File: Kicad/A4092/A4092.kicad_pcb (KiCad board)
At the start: 4 copper layers, 175.6 x 122.1 mm, 129 parts, among them CN1 Zorro3, J1 5749721-7, J2 5749721-7, J3 TO-LED, J4 TO-MB, J5 TO-A3000-LED, J6 TO-A3000-MB, J8 Conn_01x06_Pin, U1 SN74ABT16543DGGR, U10 DS21S07A, U11 DS21S07A, U12 DS21S07A, U13 W25X40CLSN, U2 SN74ABT16543DGGR, U3 SN74ABT16543DGGR, U4 SN74ABT16543DGGR, U5 74LVC07APW_118, U6 SN74ABT16245ADGGR, U7 AMS1117-3.3, U8 XC95144XL-TQ144, U9 LSI53C770 SCSI Host Controller, Y1 Abracon ACO-50MHz, Y2 Abracon ACO-40MHz

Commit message: Routing
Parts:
- moved R64 6.00 mm to (196.5, 124.0)
- moved R66 3.00 mm to (196.5, 119.5)
- moved R68 3.00 mm to (196.5, 116.5)
- moved R65 1.50 mm to (196.5, 122.5)
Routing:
- net D13: track 15.1 -> 77.5 mm, vias 0 -> 1
- net SBG: track 59.2 -> 0.00 mm, vias 1 -> 0
- net SCDATP0: track 39.5 -> 93.2 mm, vias 1 -> 2
- net A28: track 47.2 -> 99.6 mm, vias 2 -> 3
- net PLD_FC2: track 95.2 -> 147.4 mm, vias 3 -> 4
- net A30: track 44.9 -> 96.3 mm, vias 2 -> 3
- net A31: track 44.1 -> 95.0 mm, vias 2 -> 3
- net D3: track 15.3 -> 65.3 mm, vias 0 -> 1
- net D2: track 15.5 -> 64.5 mm, vias 0 -> 1
- net D5: track 15.7 -> 63.7 mm, vias 0 -> 1
- net A29: track 45.0 -> 92.9 mm, vias 2 -> 3
- net SCTRL_ATN: track 25.4 -> 72.8 mm, vias 1 -> 3
- net D4: track 15.3 -> 62.3 mm, vias 0 -> 1
- net A27: track 58.8 -> 105.5 mm, vias 4 -> 5
- net D26: track 62.0 -> 17.8 mm, vias 2 -> 0
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
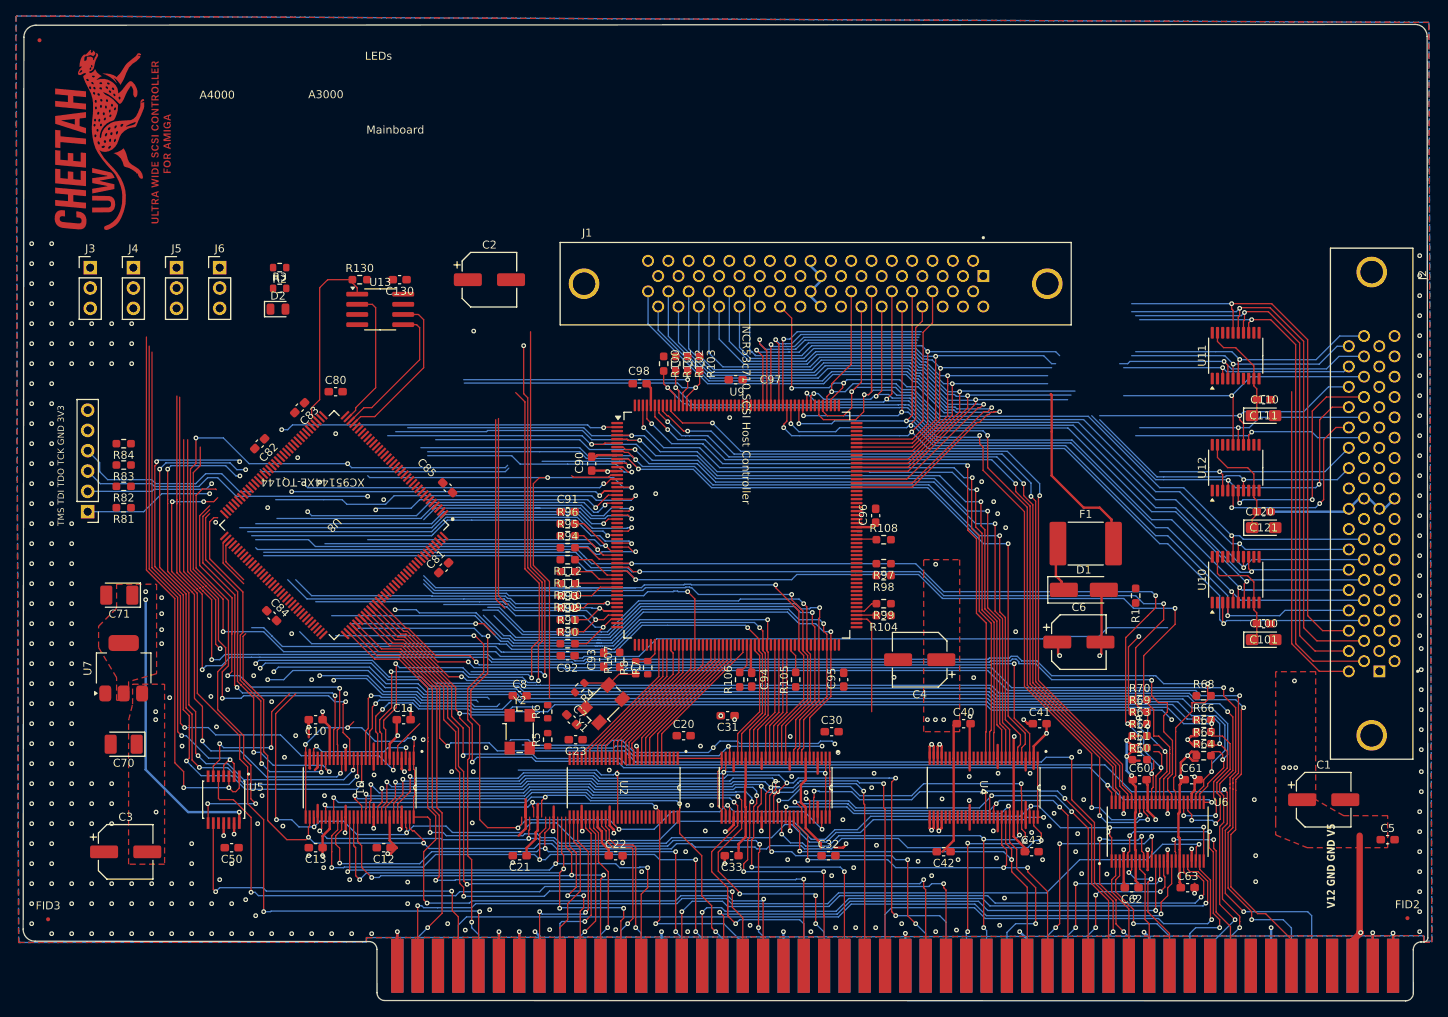
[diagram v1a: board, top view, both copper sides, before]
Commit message: CPLD Routing
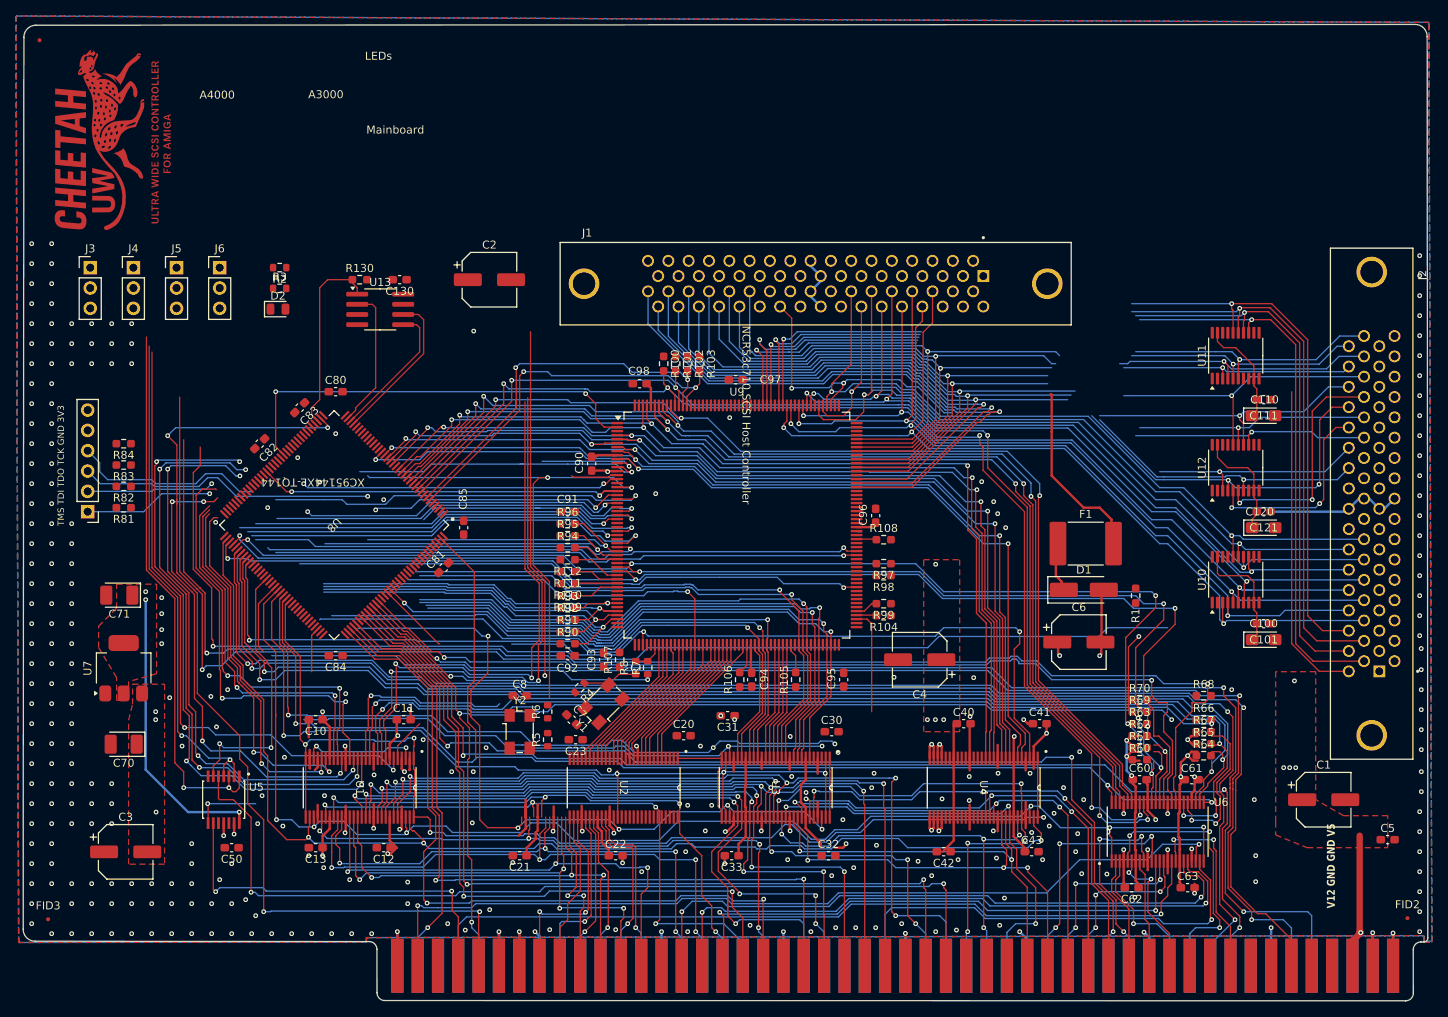
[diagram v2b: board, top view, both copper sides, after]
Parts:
- moved C84 9.43 mm to (88.0, 111.5), turned to 180 degrees
- moved C85 5.39 mm to (104.0, 95.5), turned to -90 degrees
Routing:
- net SBR: track 0.00 -> 75.0 mm, vias 0 -> 1
- net SBG: track 0.00 -> 73.4 mm, vias 0 -> 1
- net SLACK: track 0.00 -> 71.8 mm, vias 0 -> 1
- net IORST: track 99.3 -> 38.5 mm, vias 4 -> 1
- net BCLK_HALF: track 0.00 -> 58.1 mm, vias 0 -> 1
- net A5: track 95.4 -> 136.0 mm, vias 2 -> 3
- net A2: track 108.2 -> 147.8 mm, vias 4 -> 5
- net A4: track 95.3 -> 134.4 mm, vias 2 -> 3
- net A3: track 107.5 -> 146.1 mm, vias 4 -> 5
- net A6: track 95.0 -> 133.0 mm, vias 2 -> 3
- net A7: track 95.0 -> 132.5 mm, vias 2 -> 3
- net A8: track 81.8 -> 116.8 mm, vias 2 -> 3
- net A9: track 82.7 -> 117.0 mm, vias 2 -> 3
- net PLD_DS: track 34.2 -> 2.86 mm
- net BERR: track 46.4 -> 76.9 mm
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
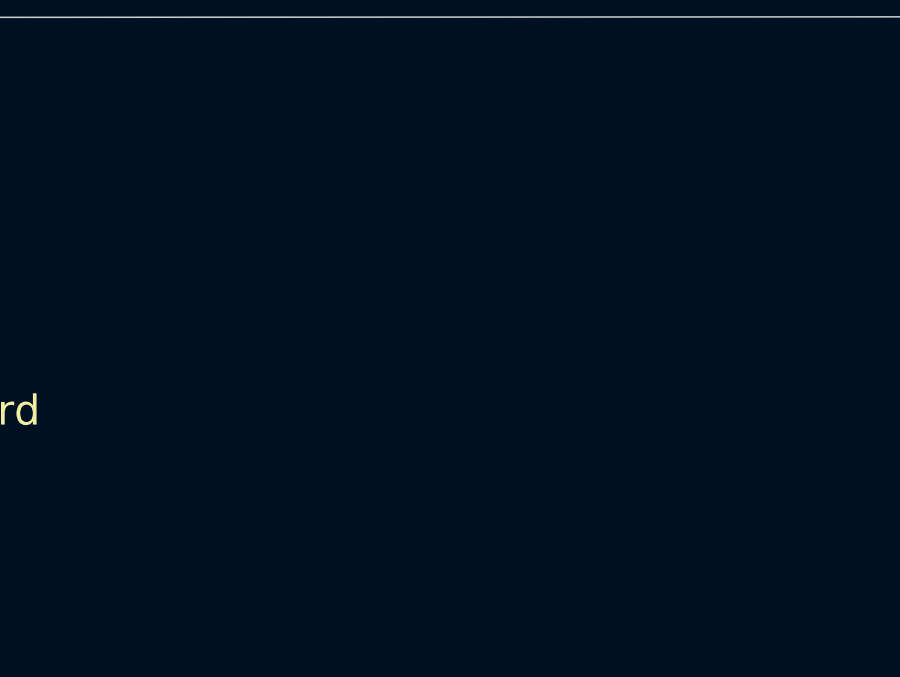
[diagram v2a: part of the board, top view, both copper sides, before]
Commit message: Update PCB from Schematic
(adds series resistors for SPI)
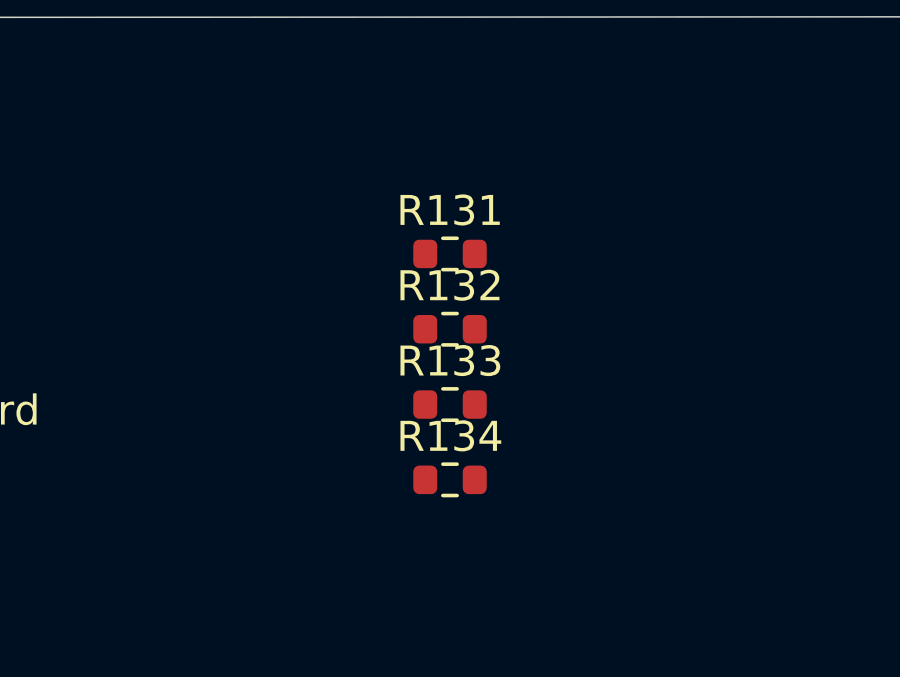
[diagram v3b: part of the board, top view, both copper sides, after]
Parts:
- added R131: 33, Resistor_SMD:R_0603_1608Metric, F.Cu at (112.7, 40.5)
- added R132: 33, Resistor_SMD:R_0603_1608Metric, F.Cu at (112.7, 43.1)
- added R133: 33, Resistor_SMD:R_0603_1608Metric, F.Cu at (112.7, 45.6)
- added R134: 33, Resistor_SMD:R_0603_1608Metric, F.Cu at (112.7, 48.1)
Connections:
- R130 pad 1: SPI_CS_n -> Net-(U13-~{CS})
- U13 pad 1: SPI_CS_n -> Net-(U13-~{CS})
- U13 pad 2: SPI_MISO -> Net-(U13-DO/IO_{1})
- U13 pad 5: SPI_MOSI -> Net-(U13-DI/IO_{0})
- U13 pad 6: SPI_CLK -> Net-(U13-CLK)
- U8 pad 49: PLD_SID -> unconnected-(U8-P49-Pad49)
- U9 pad 119: (no net) -> GND

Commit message: Undo Update PCB from Schematics
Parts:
- removed R131, R132, R133, R134: 33, Resistor_SMD:R_0603_1608Metric
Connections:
- R130 pad 1: Net-(U13-~{CS}) -> SPI_CS_n
- U13 pad 1: Net-(U13-~{CS}) -> SPI_CS_n
- U13 pad 2: Net-(U13-DO/IO_{1}) -> SPI_MISO
- U13 pad 5: Net-(U13-DI/IO_{0}) -> SPI_MOSI
- U13 pad 6: Net-(U13-CLK) -> SPI_CLK
- U8 pad 49: unconnected-(U8-P49-Pad49) -> PLD_SID
- U9 pad 119: GND -> (no net)

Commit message: CPLD Routing WIP
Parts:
- moved C81 1.58 mm to (103.0, 100.0), turned to -45 degrees
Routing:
- net D24: track 61.1 -> 25.3 mm, vias 1 -> 0
- net IORST: track 38.5 -> 72.9 mm, vias 1 -> 2
- net A26: track 83.0 -> 113.4 mm, vias 3 -> 4
- net MASTER: track 99.5 -> 128.9 mm, vias 4 -> 5
- net A16: track 62.0 -> 88.0 mm, vias 2 -> 5
- net TDO: track 37.2 -> 16.3 mm, vias 1 -> 0
- net A22: track 56.7 -> 72.2 mm
- net PLD_DOE: track 174.9 -> 190.2 mm, vias 2 -> 4
- net D2Z: track 69.1 -> 82.0 mm
- net A18: track 71.9 -> 84.2 mm, vias 2 -> 4
- net D31: track 18.0 -> 29.3 mm
- net D30: track 18.0 -> 29.0 mm
- net CBACK: track 43.3 -> 54.2 mm, vias 1 -> 2
- net D29: track 17.8 -> 27.9 mm
- net A20: track 92.1 -> 102.2 mm, vias 3 -> 4
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
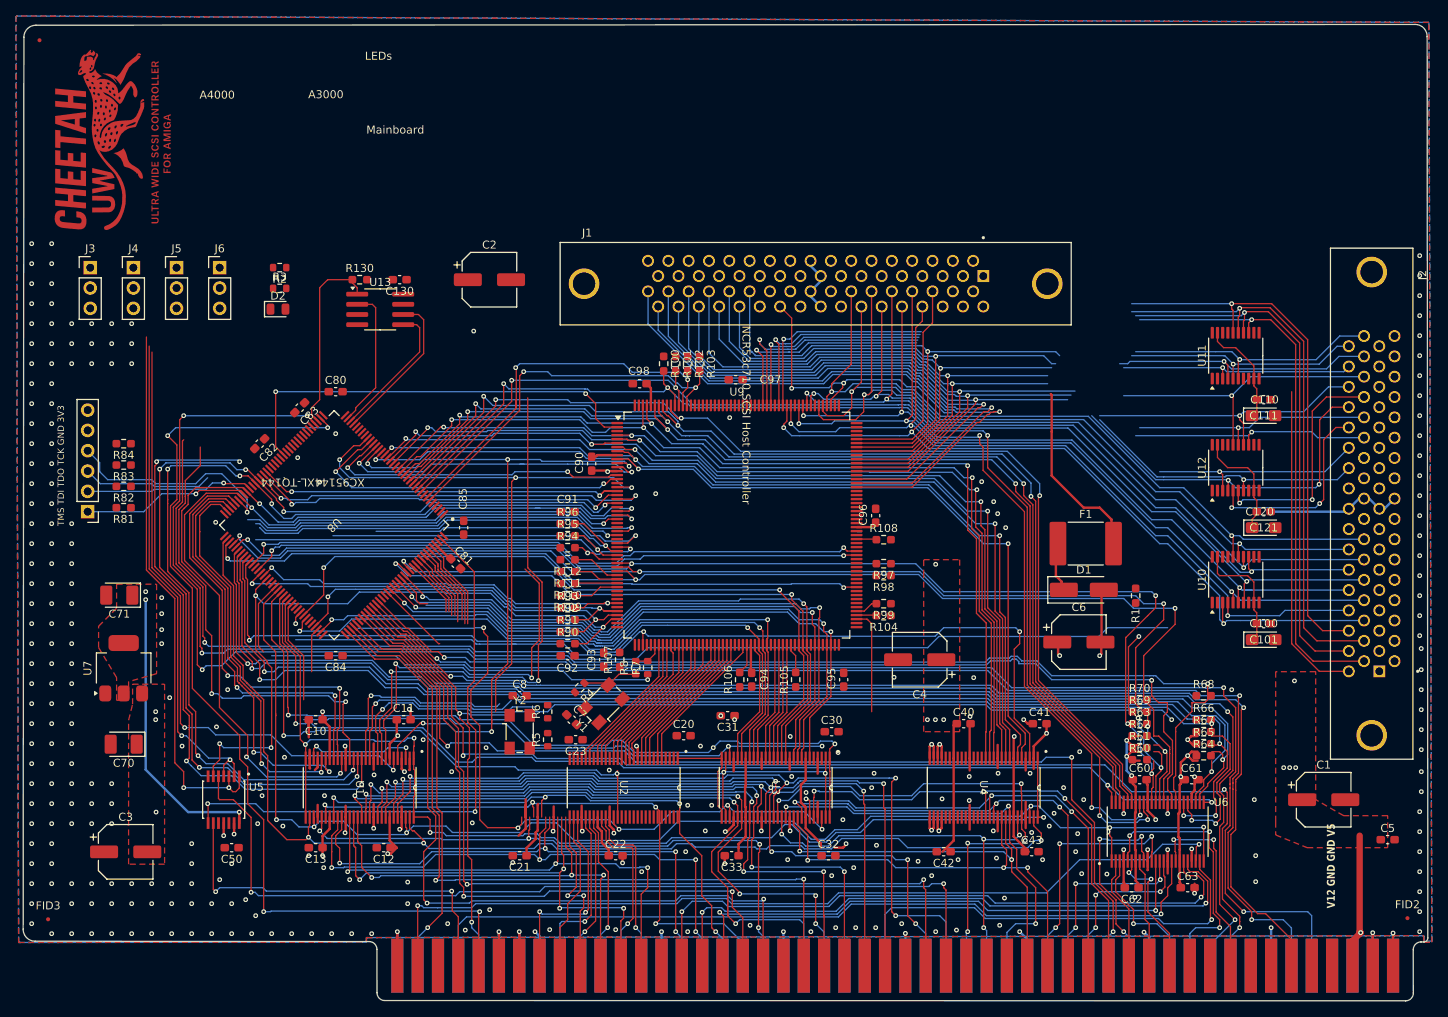
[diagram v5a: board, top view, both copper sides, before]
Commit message: Imported netlist and general routing
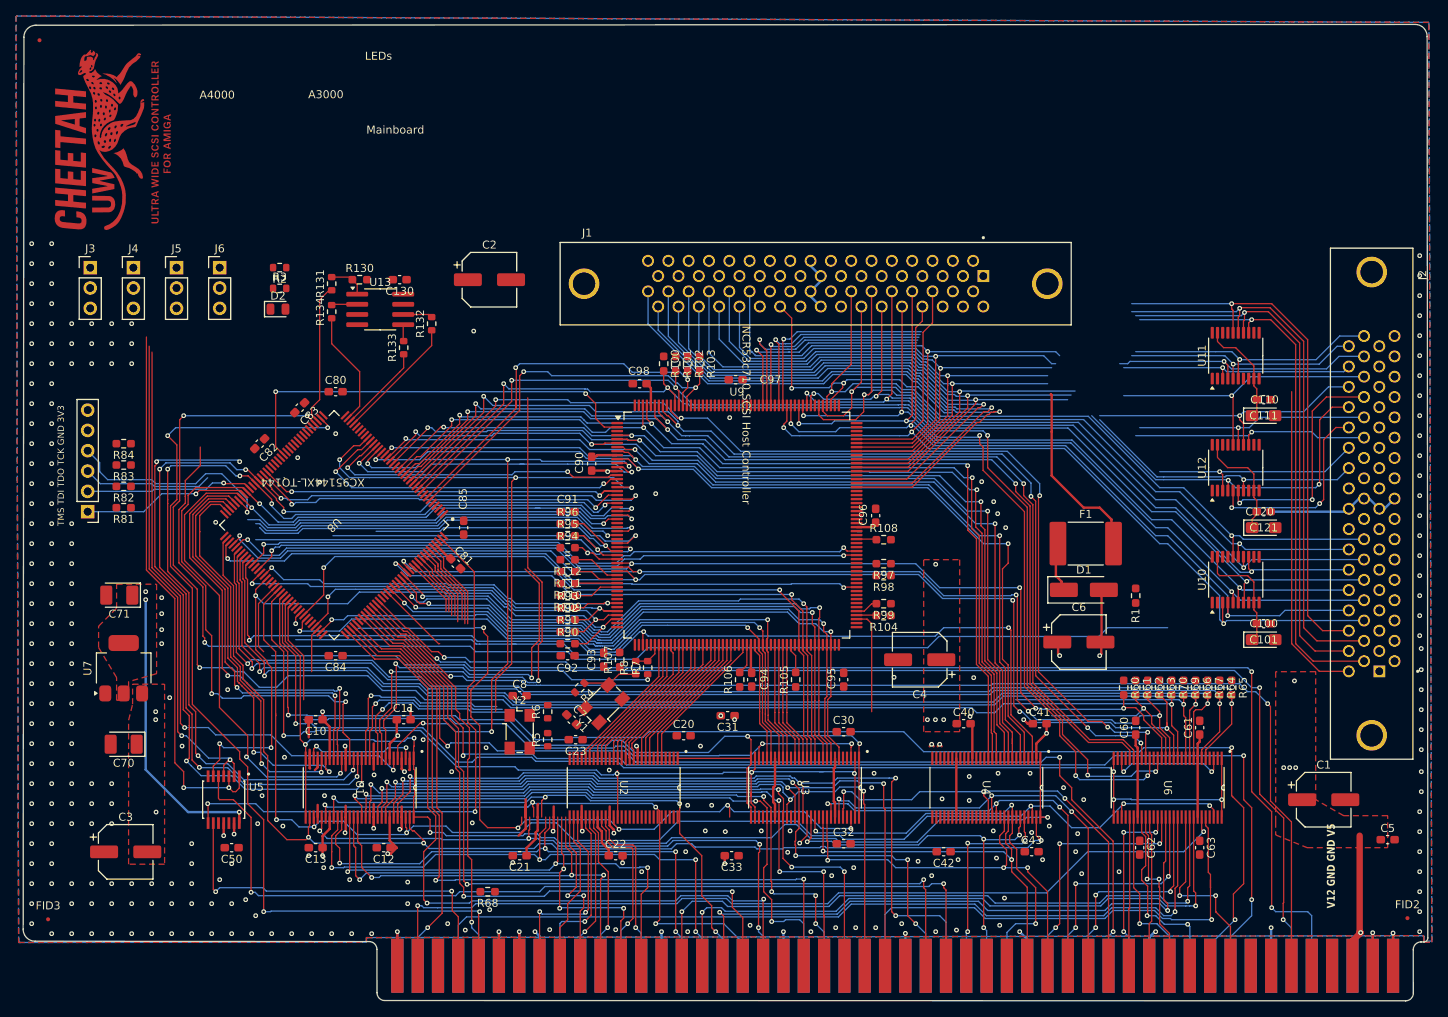
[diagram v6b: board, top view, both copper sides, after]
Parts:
- added R131: 33, Resistor_SMD:R_0603_1608Metric, F.Cu at (87.5, 65.0)
- added R132: 33, Resistor_SMD:R_0603_1608Metric, F.Cu at (100.0, 70.0)
- added R133: 33, Resistor_SMD:R_0603_1608Metric, F.Cu at (96.5, 73.0)
- added R134: 0, Resistor_SMD:R_0603_1608Metric, F.Cu at (87.5, 68.5)
- U6: value SN74ABT16245ADGGR -> SN74ABT16543DGGR; footprint SN74ABT16245ADGGR:DGG48 -> SN74ABT16543DGGR:DGG56
- moved R68 92.8 mm to (107.0, 141.0), turned to 180 degrees
- moved R60 9.22 mm to (186.5, 115.5), turned to -90 degrees
- moved R64 8.73 mm to (198.5, 115.5), turned to -90 degrees
- moved R65 7.83 mm to (200.0, 115.5), turned to -90 degrees
- moved R61 7.52 mm to (188.0, 115.5), turned to -90 degrees
- moved C61 6.58 mm to (196.0, 120.5), turned to 90 degrees
- moved C60 6.52 mm to (188.0, 120.5), turned to 90 degrees
- moved R69 6.26 mm to (194.0, 115.5), turned to -90 degrees
- moved R62 6.08 mm to (189.5, 115.5), turned to -90 degrees
- moved U6 5.64 mm to (192.0, 128.0), turned to -90 degrees
- moved R67 5.52 mm to (197.0, 115.5), turned to -90 degrees
- moved C63 5.22 mm to (196.0, 135.5), turned to -90 degrees
- moved R63 5.15 mm to (191.0, 115.5), turned to -90 degrees
- moved C62 5.10 mm to (188.5, 135.5), turned to -90 degrees
- moved R70 4.27 mm to (192.5, 115.5), turned to -90 degrees
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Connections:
- R130 pad 1: SPI_CS_n -> Net-(U13-~{CS})
- U13 pad 1: SPI_CS_n -> Net-(U13-~{CS})
- U13 pad 2: SPI_MISO -> Net-(U13-DO/IO_{1})
- U13 pad 5: SPI_MOSI -> Net-(U13-DI/IO_{0})
- U13 pad 6: SPI_CLK -> Net-(U13-CLK)
- U6 pad 1: BMASTER -> ABOEL
- U6 pad 10: GND -> PLD_MTCR
- U6 pad 11: Z_FC2 -> GND
- U6 pad 12: Z_READ -> PLD_DOE
- U6 pad 13: Z_FC1 -> PLD_FC0
- U6 pad 14: Z_FC0 -> PLD_FC1
- U6 pad 15: GND -> PLD_READ
- U6 pad 16: Z_DOE -> PLD_FC2
- U6 pad 17: Z_MTCR -> A2
- U6 pad 18: V5 -> GND
- U6 pad 19: Z_DS3 -> A3
- U6 pad 2: Z_A7 -> GND
- U6 pad 20: Z_DS2 -> A4
- U6 pad 21: GND -> A5
- U6 pad 22: Z_DS1 -> V5
- U6 pad 23: Z_DS0 -> A6
- U6 pad 24: BMASTER -> A7
- U6 pad 25: ABOEL -> GND
- U6 pad 26: PLD_DS0 -> MASTER
- U6 pad 27: PLD_DS1 -> GND
- U6 pad 28: GND -> ABOEL
- U6 pad 29: PLD_DS2 -> ABOEL
- U6 pad 3: Z_A6 -> MASTER
- U6 pad 30: PLD_DS3 -> GND
- U6 pad 31: V5 -> BMASTER
- U6 pad 32: PLD_MTCR -> GND
- U6 pad 33: PLD_DOE -> Z_A7
- U6 pad 34: GND -> Z_A6
- U6 pad 35: PLD_FC0 -> V5
- U6 pad 36: PLD_FC1 -> Z_A5
- U6 pad 37: PLD_READ -> Z_A4
- U6 pad 38: PLD_FC2 -> Z_A3
- U6 pad 40: A2 -> Z_A2
- U6 pad 41: A3 -> Z_FC2
- U6 pad 42: V5 -> Z_READ
- U6 pad 43: A4 -> Z_FC1
- U6 pad 44: A5 -> Z_FC0
- U6 pad 45: GND -> Z_DOE
- U6 pad 46: A6 -> GND
- U6 pad 47: A7 -> Z_MTCR
- U6 pad 48: ABOEL -> Z_DS3
- U6 pad 5: Z_A5 -> PLD_DS0
- U6 pad 6: Z_A4 -> PLD_DS1
- U6 pad 8: Z_A3 -> PLD_DS2
- U6 pad 9: Z_A2 -> PLD_DS3
- U8 pad 49: PLD_SID -> unconnected-(U8-P49-Pad49)
- U9 pad 119: (no net) -> GND
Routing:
- net PLD_MTCR: track 174.4 -> 29.3 mm, vias 2 -> 1
- net Z_SENSEZ3: track 141.2 -> 50.8 mm, vias 3 -> 1
- net GND: track 207.4 -> 139.8 mm, vias 319 -> 294
- net V5: track 256.0 -> 193.6 mm, vias 29 -> 21
- net Z_A15D7: track 64.4 -> 29.4 mm, vias 5 -> 4
- net MASTER: track 128.9 -> 143.3 mm, vias 5 -> 7
- net Z_INT2: track 142.0 -> 128.3 mm
- net PLD_DS3: track 157.5 -> 144.0 mm, vias 4 -> 2
- net PLD_DS2: track 159.9 -> 146.9 mm, vias 4 -> 2
- net ABOEL: track 139.1 -> 150.5 mm, vias 3 -> 4
- net Z_A5: track 34.1 -> 23.9 mm, vias 3 -> 2
- net PLD_FC2: track 152.1 -> 141.9 mm
- net DBOE: track 110.1 -> 119.9 mm
- net Z_READ: track 68.9 -> 76.9 mm
- net Z_DOE: track 101.9 -> 109.4 mm
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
